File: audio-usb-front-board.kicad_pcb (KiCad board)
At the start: 2 copper layers, 70.7 x 20 mm, 5 parts, among them J1 USB_A_right, J2 USB_A_left, J3 AudioJack3_SwitchTR_output, J4 AudioJack3_SwitchTR_mic, J5 Conn_01x16

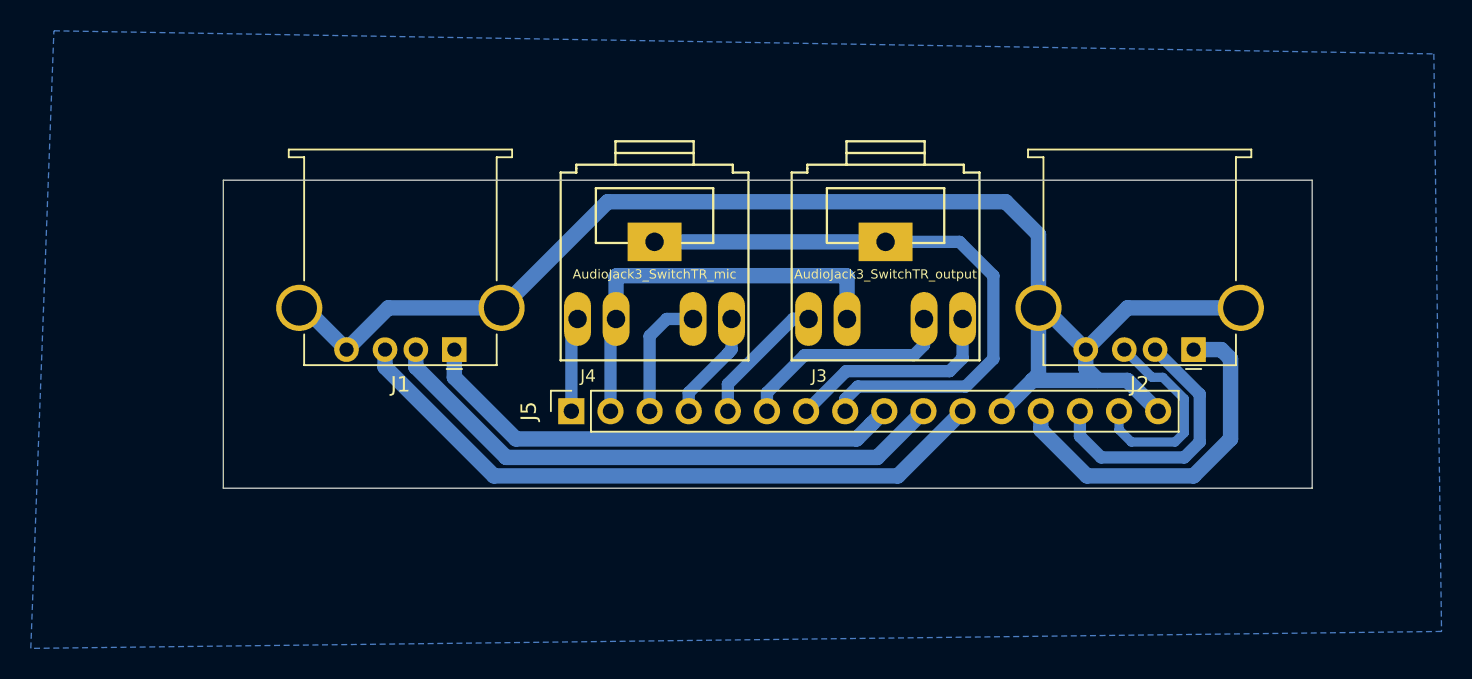
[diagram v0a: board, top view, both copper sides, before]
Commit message: change sch a bit, change pad sizes
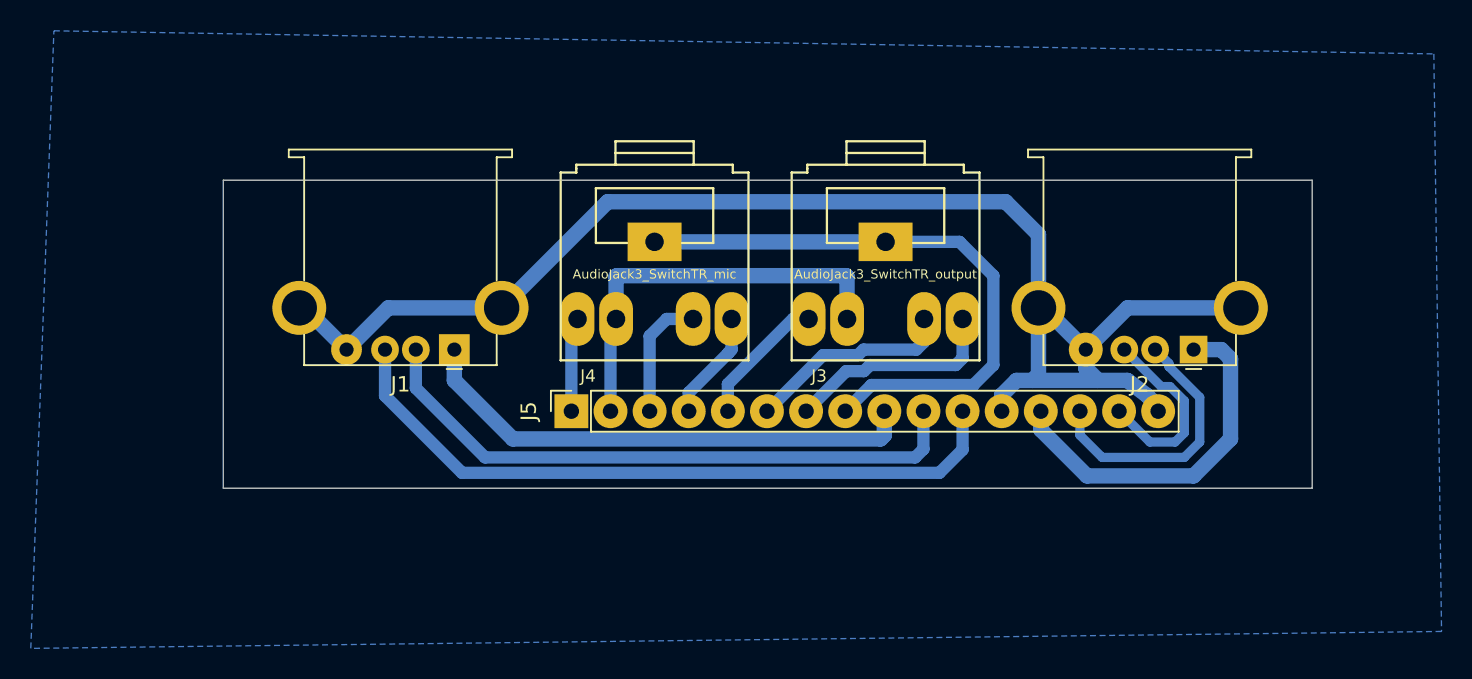
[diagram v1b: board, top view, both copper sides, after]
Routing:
- net Net-(J1-Pad3): track 43.3 -> 45.7 mm
- net Net-(J1-Pad2): track 37.8 -> 40.0 mm
- net Net-(J1-Pad1): track 32.2 -> 33.3 mm
- net Net-(J3-PadRN): track 14.4 -> 13.6 mm
- net Net-(J2-Pad3): track 13.4 -> 12.7 mm
- net GND: track 93.1 -> 93.9 mm
